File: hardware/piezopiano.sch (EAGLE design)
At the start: 102 parts, among them J2 CON2, Q1 DMN3404L, Q2 DMN3404L, Q3 DMN3404L, Q4 DMN3404L, Q5 DMN3404L, Q6 DMN3404L, Q7 DMN3404L, Q8 DMN3404L, Q9 DNP, U1 CH340E_MSOP10, U2 ATMEGA4809, U3 MSP432P401RIZXHR

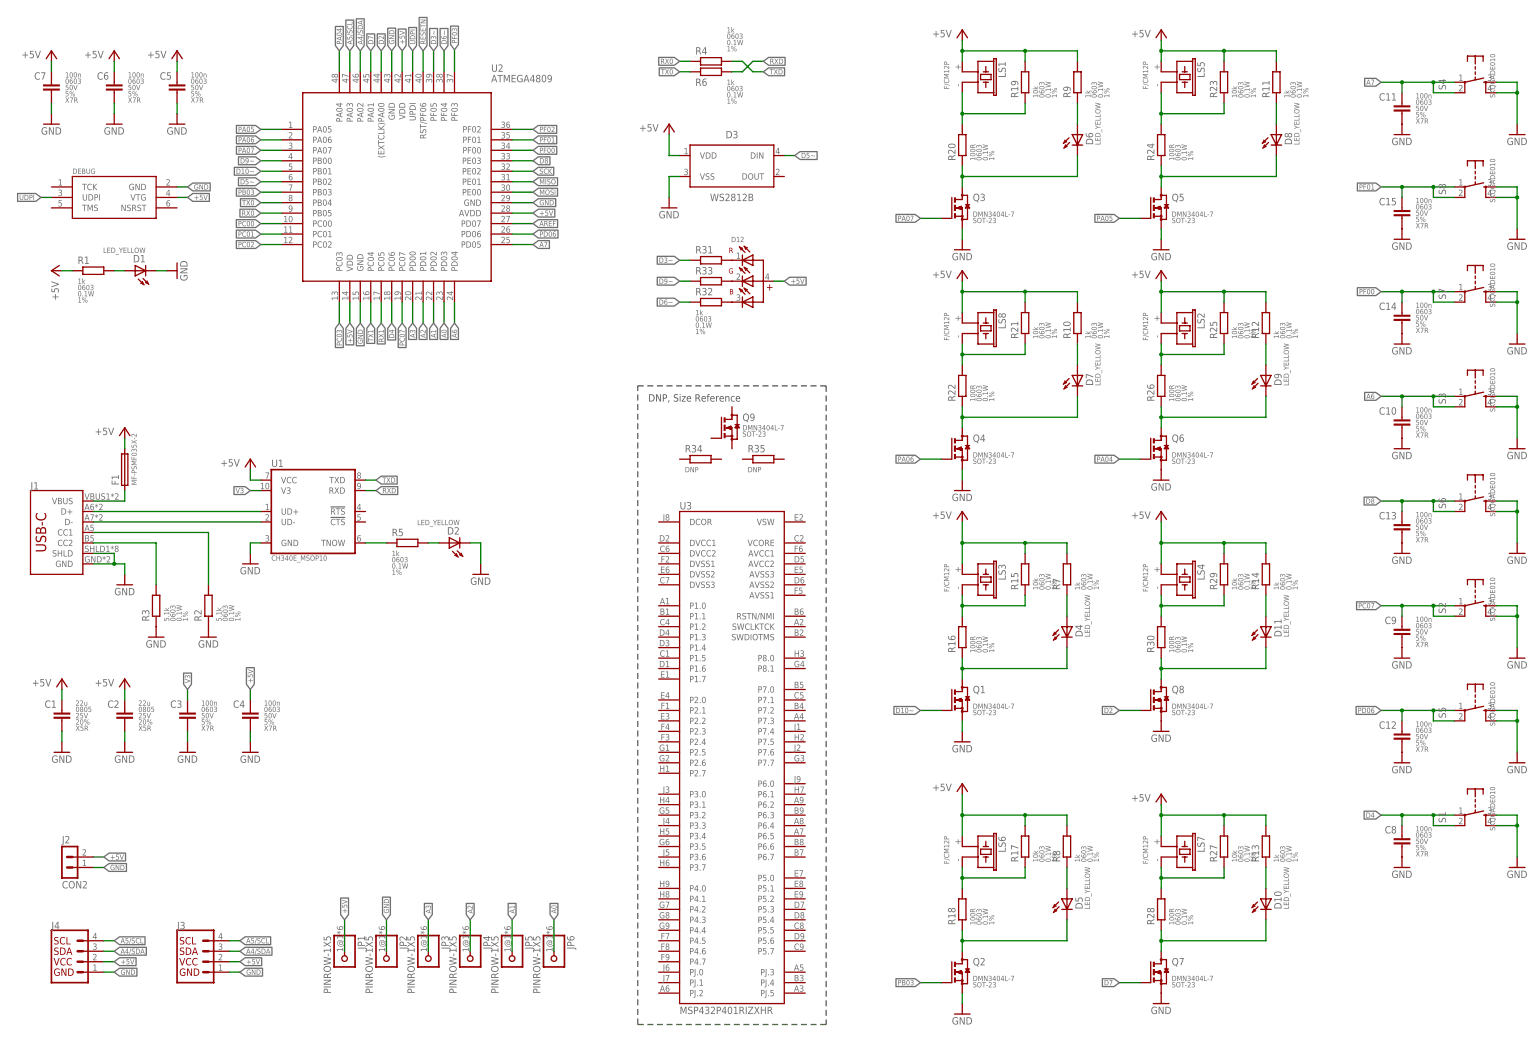
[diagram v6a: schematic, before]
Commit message: Added images and updated device data
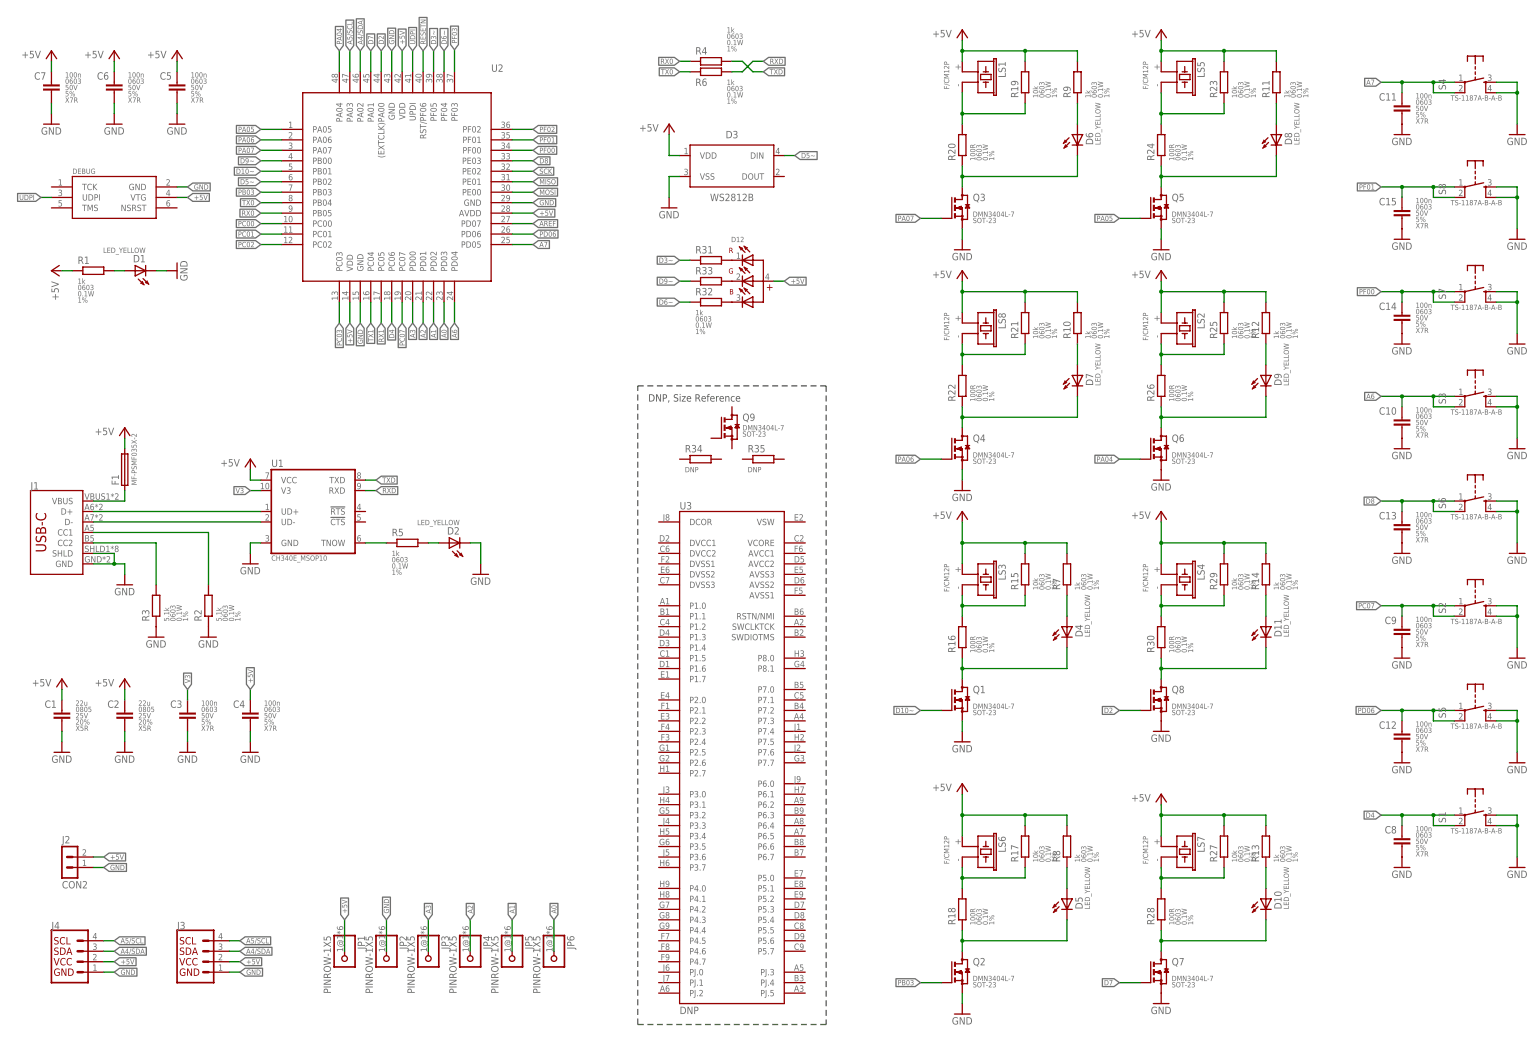
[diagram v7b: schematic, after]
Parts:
- S1, S2, S3, S4, S5, S6, S7, S8: value SKQGADE010 -> TS-1187A-B-A-B; device zaan-Electromechanical:SKQGADE010 -> zaan-Electromechanical:TS-1187A-B-A-B
- U3: value MSP432P401RIZXHR -> DNP
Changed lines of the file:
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@@
 </classes>
 <parts>
-<part name="S4" library="zaan-Electromechanical" library_urn="urn:adsk.eagle:library:16759157" deviceset="SKQGADE010" device="" package3d_urn="urn:adsk.eagle:package:16672570/3"/>
-<part name="S8" library="zaan-Electromechanical" library_urn="urn:adsk.eagle:library:16759157" deviceset="SKQGADE010" device="" package3d_urn="urn:adsk.eagle:package:16672570/3"/>
-<part name="S3" library="zaan-Electromechanical" library_urn="urn:adsk.eagle:library:16759157" deviceset="SKQGADE010" device="" package3d_urn="urn:adsk.eagle:package:16672570/3"/>
-<part name="S7" library="zaan-Electromechanical" library_urn="urn:adsk.eagle:library:16759157" deviceset="SKQGADE010" device="" package3d_urn="urn:adsk.eagle:package:16672570/3"/>
-<part name="S2" library="zaan-Electromechanical" library_urn="urn:adsk.eagle:library:16759157" deviceset="SKQGADE010" device="" package3d_urn="urn:adsk.eagle:package:16672570/3"/>
-<part name="S6" library="zaan-Electromechanical" library_urn="urn:adsk.eagle:library:16759157" deviceset="SKQGADE010" device="" package3d_urn="urn:adsk.eagle:package:16672570/3"/>
-<part name="S1" library="zaan-Electromechanical" library_urn="urn:adsk.eagle:library:16759157" deviceset="SKQGADE010" device="" package3d_urn="urn:adsk.eagle:package:16672570/3"/>
-<part name="S5" library="zaan-Electromechanical" library_urn="urn:adsk.eagle:library:16759157" deviceset="SKQGADE010" device="" package3d_urn="urn:adsk.eagle:package:16672570/3"/>
+<part name="S4" library="zaan-Electromechanical" library_urn="urn:adsk.eagle:library:16759157" deviceset="TS-1187A-B-A-B" device="" package3d_urn="urn:adsk.eagle:package:16672570/3"/>
+<part name="S8" library="zaan-Electromechanical" library_urn="urn:adsk.eagle:library:16759157" deviceset="TS-1187A-B-A-B" device="" package3d_urn="urn:adsk.eagle:package:16672570/3"/>
+<part name="S3" library="zaan-Electromechanical" library_urn="urn:adsk.eagle:library:16759157" deviceset="TS-1187A-B-A-B" device="" package3d_urn="urn:adsk.eagle:package:16672570/3"/>
+<part name="S7" library="zaan-Electromechanical" library_urn="urn:adsk.eagle:library:16759157" deviceset="TS-1187A-B-A-B" device="" package3d_urn="urn:adsk.eagle:package:16672570/3"/>
+<part name="S2" library="zaan-Electromechanical" library_urn="urn:adsk.eagle:library:16759157" deviceset="TS-1187A-B-A-B" device="" package3d_urn="urn:adsk.eagle:package:16672570/3"/>
+<part name="S6" library="zaan-Electromechanical" library_urn="urn:adsk.eagle:library:16759157" deviceset="TS-1187A-B-A-B" device="" package3d_urn="urn:adsk.eagle:package:16672570/3"/>
+<part name="S1" library="zaan-Electromechanical" library_urn="urn:adsk.eagle:library:16759157" deviceset="TS-1187A-B-A-B" device="" package3d_urn="urn:adsk.eagle:package:16672570/3"/>
+<part name="S5" library="zaan-Electromechanical" library_urn="urn:adsk.eagle:library:16759157" deviceset="TS-1187A-B-A-B" device="" package3d_urn="urn:adsk.eagle:package:16672570/3"/>
 <part name="Q3" library="zaan-Discrete" library_urn="urn:adsk.eagle:library:16759095" deviceset="DMN3404L" device="" package3d_urn="urn:adsk.eagle:package:16759132/2"/>
 <part name="Q4" library="zaan-Discrete" library_urn="urn:adsk.eagle:library:16759095" deviceset="DMN3404L" device="" package3d_urn="urn:adsk.eagle:package:16759132/2"/>
@@
 <part name="R34" library="zaan-Resistors" library_urn="urn:adsk.eagle:library:16759442" deviceset="DNP" device="-0805" package3d_urn="urn:adsk.eagle:package:16759454/7" value="DNP"/>
 <part name="Q9" library="zaan-Discrete" library_urn="urn:adsk.eagle:library:16759095" deviceset="DMN3404L" device="" package3d_urn="urn:adsk.eagle:package:16759132/2" value="DNP"/>
-<part name="U3" library="zaan-IC-Microcontroller" library_urn="urn:adsk.eagle:library:16759236" deviceset="MSP432P401RIZXHR" device="" package3d_urn="urn:adsk.eagle:package:31294788/1"/>
+<part name="U3" library="zaan-IC-Microcontroller" library_urn="urn:adsk.eagle:library:16759236" deviceset="MSP432P401RIZXHR" device="" package3d_urn="urn:adsk.eagle:package:31294788/1" value="DNP"/>
 <part name="R33" library="zaan-Resistors" library_urn="urn:adsk.eagle:library:16759442" deviceset="1KOHM" device="-0603-1/10W-1%" package3d_urn="urn:adsk.eagle:package:16759452/3" value="1k"/>
 <part name="R31" library="zaan-Resistors" library_urn="urn:adsk.eagle:library:16759442" deviceset="1KOHM" device="-0603-1/10W-1%" package3d_urn="urn:adsk.eagle:package:16759452/3" value="1k"/>
@@
 <instance part="S4" gate="G$1" x="363.22" y="236.22" smashed="yes">
 <attribute name="NAME" x="355.219" y="234.315" size="1.778" layer="95" rot="R90" align="center-left"/>
-<attribute name="VALUE" x="367.411" y="232.41" size="1.27" layer="96" rot="R90" align="center-left"/>
+<attribute name="VALUE" x="357.251" y="232.41" size="1.27" layer="96" align="center-left"/>
 </instance>
 <instance part="S8" gate="G$1" x="363.22" y="210.82" smashed="yes">
 <attribute name="NAME" x="355.219" y="208.915" size="1.778" layer="95" rot="R90" align="center-left"/>
-<attribute name="VALUE" x="367.411" y="207.01" size="1.27" layer="96" rot="R90" align="center-left"/>
+<attribute name="VALUE" x="357.251" y="207.01" size="1.27" layer="96" align="center-left"/>
 </instance>
 <instance part="S3" gate="G$1" x="363.22" y="160.02" smashed="yes">
 <attribute name="NAME" x="355.219" y="158.115" size="1.778" layer="95" rot="R90" align="center-left"/>
-<attribute name="VALUE" x="367.411" y="156.21" size="1.27" layer="96" rot="R90" align="center-left"/>
+<attribute name="VALUE" x="357.251" y="156.21" size="1.27" layer="96" align="center-left"/>
 </instance>
 <instance part="S7" gate="G$1" x="363.22" y="185.42" smashed="yes">
 <attribute name="NAME" x="355.219" y="183.515" size="1.778" layer="95" rot="R90" align="center-left"/>
-<attribute name="VALUE" x="367.411" y="181.61" size="1.27" layer="96" rot="R90" align="center-left"/>
+<attribute name="VALUE" x="357.251" y="181.61" size="1.27" layer="96" align="center-left"/>
 </instance>
 <instance part="S2" gate="G$1" x="363.22" y="109.22" smashed="yes">
 <attribute name="NAME" x="355.219" y="107.315" size="1.778" layer="95" rot="R90" align="center-left"/>
-<attribute name="VALUE" x="367.411" y="105.41" size="1.27" layer="96" rot="R90" align="center-left"/>
+<attribute name="VALUE" x="357.251" y="105.41" size="1.27" layer="96" align="center-left"/>
 </instance>
 <instance part="S6" gate="G$1" x="363.22" y="134.62" smashed="yes">
 <attribute name="NAME" x="355.219" y="132.715" size="1.778" layer="95" rot="R90" align="center-left"/>
-<attribute name="VALUE" x="367.411" y="130.81" size="1.27" layer="96" rot="R90" align="center-left"/>
+<attribute name="VALUE" x="357.251" y="130.81" size="1.27" layer="96" align="center-left"/>
 </instance>
 <instance part="S1" gate="G$1" x="363.22" y="58.42" smashed="yes">
 <attribute name="NAME" x="355.219" y="56.515" size="1.778" layer="95" rot="R90" align="center-left"/>
-<attribute name="VALUE" x="367.411" y="54.61" size="1.27" layer="96" rot="R90" align="center-left"/>
+<attribute name="VALUE" x="357.251" y="54.61" size="1.27" layer="96" align="center-left"/>
 </instance>
 <instance part="S5" gate="G$1" x="363.22" y="83.82" smashed="yes">
 <attribute name="NAME" x="355.219" y="81.915" size="1.778" layer="95" rot="R90" align="center-left"/>
-<attribute name="VALUE" x="367.411" y="80.01" size="1.27" layer="96" rot="R90" align="center-left"/>
+<attribute name="VALUE" x="357.251" y="80.01" size="1.27" layer="96" align="center-left"/>
 </instance>
 <instance part="Q3" gate="G$1" x="238.76" y="205.74" smashed="yes">
@@
 <instance part="U2" gate="G$1" x="101.6" y="210.82" smashed="yes">
 <attribute name="NAME" x="124.46" y="238.76" size="1.778" layer="95"/>
-<attribute name="VALUE" x="124.46" y="236.22" size="1.778" layer="96"/>
 </instance>
 <instance part="DEBUG" gate="G$1" x="33.02" y="208.28" smashed="yes">

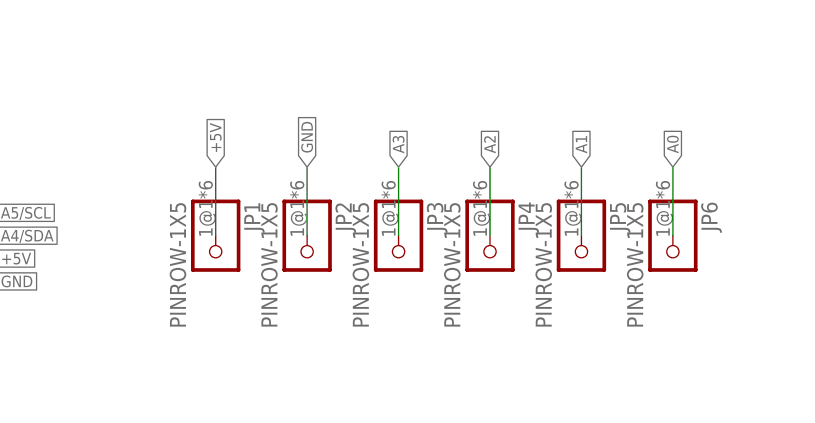
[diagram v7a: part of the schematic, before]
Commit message: Reverted to local libraries
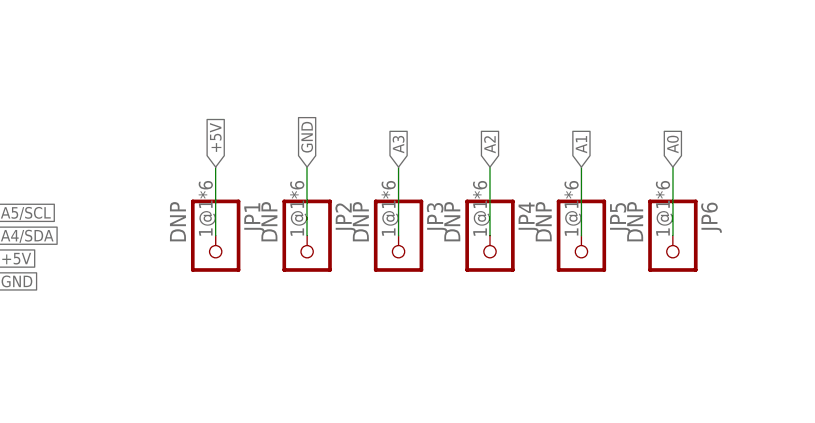
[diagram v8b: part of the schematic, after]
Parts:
- DEBUG: value AVR-UPDI-6-SKEDD -> DNP
- JP1, JP2, JP3, JP4, JP5, JP6: value PINROW-1X5 -> DNP
